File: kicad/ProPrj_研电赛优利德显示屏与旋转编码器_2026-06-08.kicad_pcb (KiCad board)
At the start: 2 copper layers, 75 x 45 mm, 16 parts, among them Q1 S8050, SW1 EC11N1525405, U1 ST7789_12P_LCD

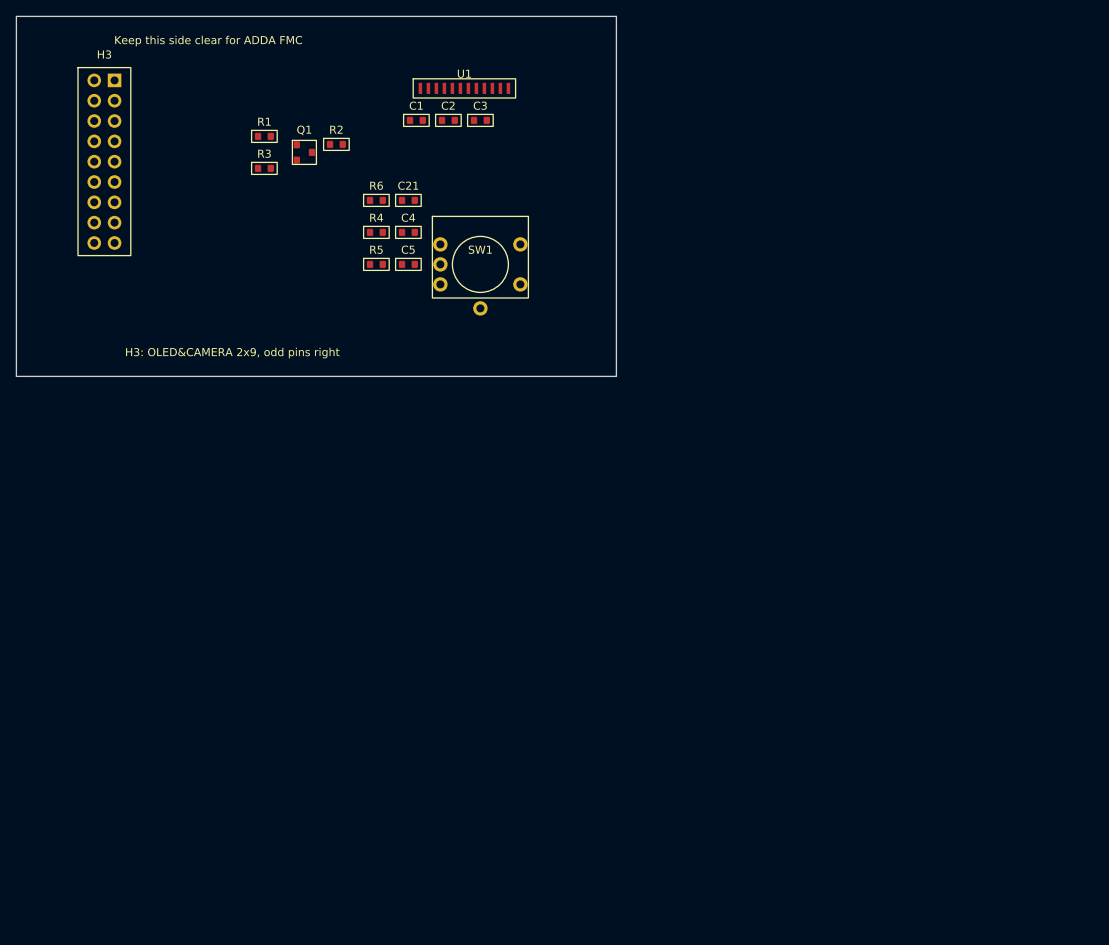
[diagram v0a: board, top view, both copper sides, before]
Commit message: perf: fix gated clock and DSP pipeline warnings
1. SPI gated clock (PDRC-153):
   - Replace posedge r_sclk with posedge clk_in + edge detection enable
   - Removes derived clock domain, uses main clk_in for all registers

2. DSP pipeline (DPIP-1/DPOP-2):
   - Add raw0_s1b..raw3_s1b pipeline registers between waveform mux and
     multiplier, enabling DSP48 AREG/BREG usage (DPIP-1: FIXED)
   - DPOP-2 (MREG) remains: DSP internal product register not used,
     timing still met at 250MHz

3. Results: 20 warnings -> 11 warnings
   - DSP: 8 -> 4 (DPIP-1 fixed, DPOP-2 remains minor)
   - Gated clock: 3 -> 3 (now false positive after fix)
   - ILA LUT/no-load: 6 -> 4 (Vivado IP internal, unfixable)

Co-Authored-By: Claude Opus 4.8 <noreply@anthropic.com>
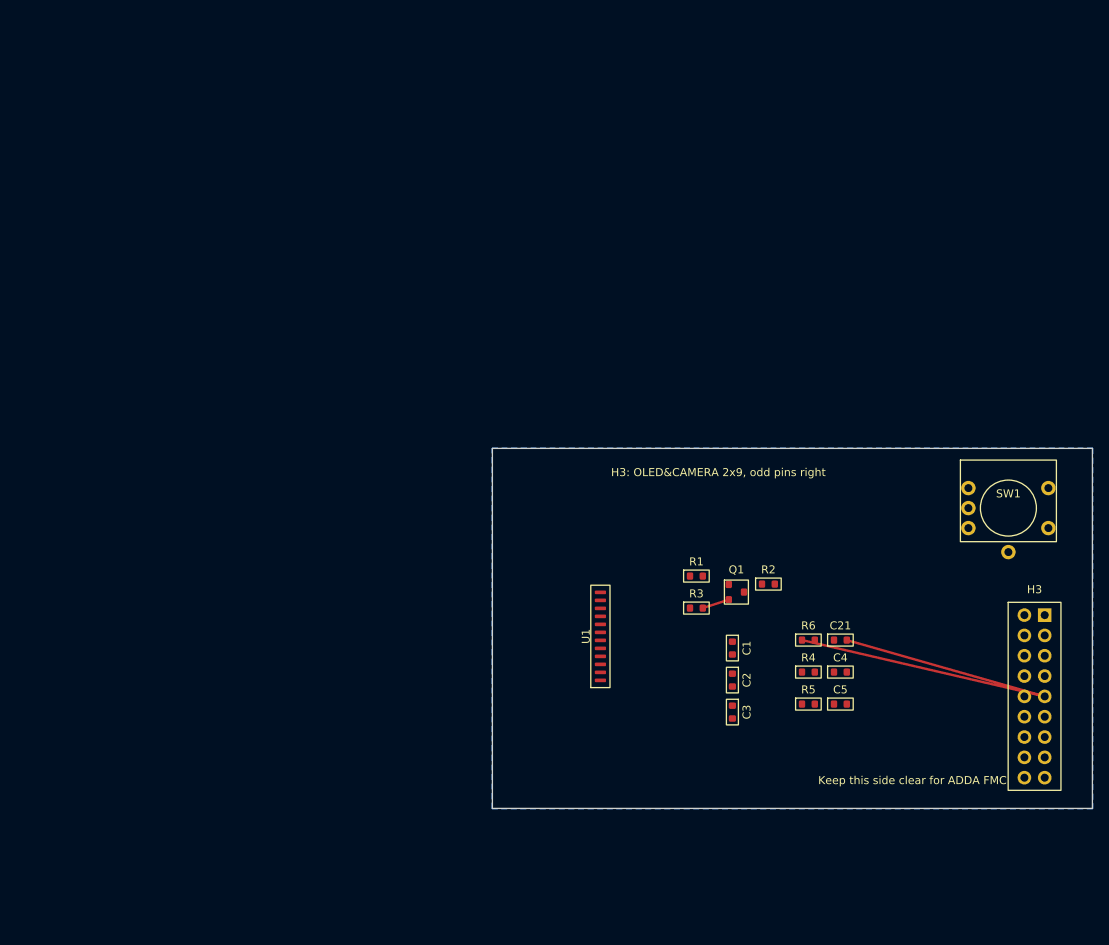
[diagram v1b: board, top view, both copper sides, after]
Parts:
- moved H3 134.1 mm to (127.3, 74.8)
- moved C3 80.4 mm to (89.5, 87.0), turned to -90 degrees
- moved C2 78.5 mm to (89.5, 83.0), turned to -90 degrees
- moved C21 77.0 mm to (103.0, 78.0)
- moved C4 77.0 mm to (103.0, 82.0)
- moved C5 77.0 mm to (103.0, 86.0)
- moved Q1 77.0 mm to (90.0, 72.0)
- moved R1 77.0 mm to (85.0, 70.0)
- moved R2 77.0 mm to (94.0, 71.0)
- moved R3 77.0 mm to (85.0, 74.0)
- moved R4 77.0 mm to (99.0, 82.0)
- moved R5 77.0 mm to (99.0, 86.0)
- moved R6 77.0 mm to (99.0, 78.0)
- moved C1 76.9 mm to (89.5, 79.0), turned to -90 degrees
- moved SW1 72.7 mm to (124.0, 61.5)
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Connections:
- net /TFT_BLK renamed TFT_BLK
- net /TFT_CS renamed TFT_CS
- net /TFT_DC renamed TFT_DC
- net /TFT_RES renamed TFT_RES
- net /TFT_SCL renamed TFT_SCL
- net /TFT_SDA renamed TFT_SDA
- H3 pad 10: /EC11-B -> EC11-B
- H3 pad 11: /EC11-M -> EC11-M
- H3 pad 12: /LEDK -> LEDK
- H3 pad 9: /EC11-A -> EC11-A
- SW1 pad A: /EC11-A -> EC11-A
- SW1 pad B: /EC11-B -> EC11-B
- SW1 pad D: /EC11-M -> EC11-M
- U1 pad 2: /LEDK -> LEDK
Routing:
- net /EC11-A: track 0.00 -> 56.9 mm
- net Net-(Q1-B): track 0.00 -> 3.42 mm
- added copper zone on B.Cu, net GND

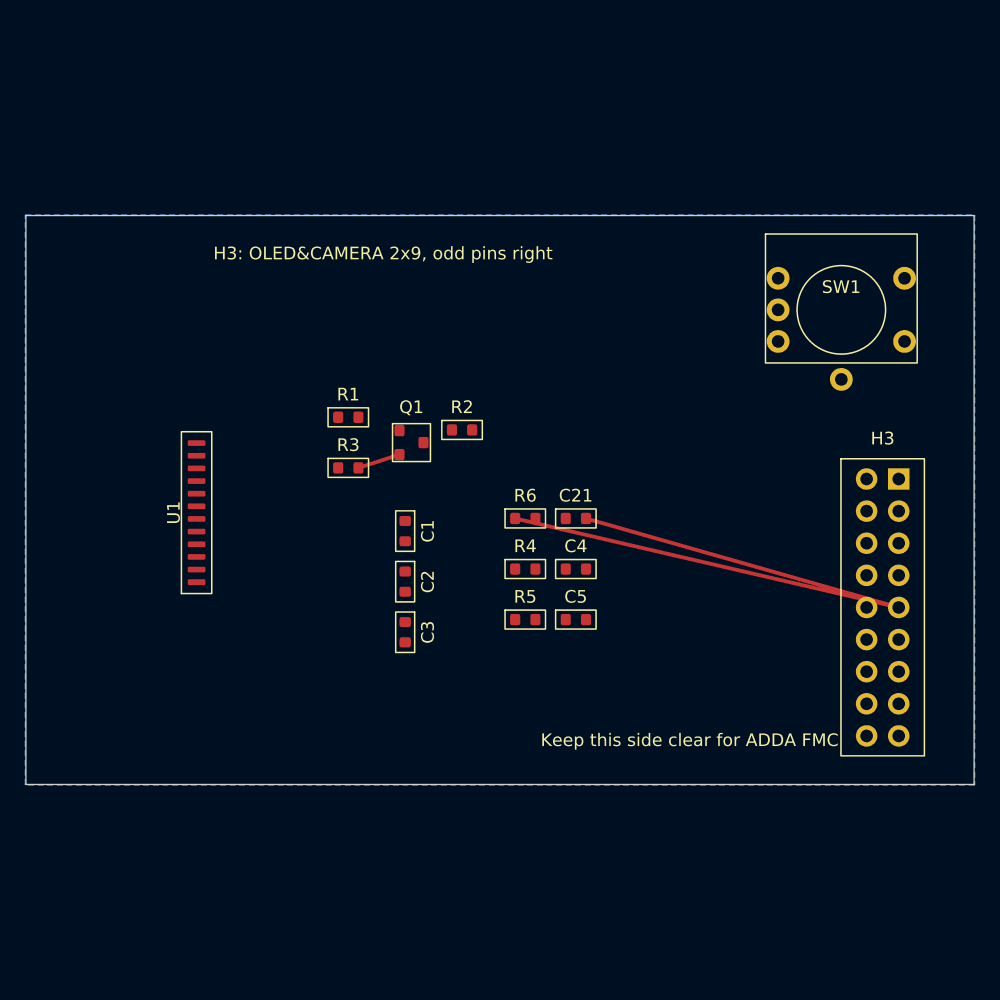
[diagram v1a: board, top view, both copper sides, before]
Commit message: perf: SPI robustness and obsidian cleanup
1. SPI gated clock: remove edge detector, use counter tick (spi_tick)
2. Suppress PDRC-153 (Vivado 2024.1 FSM false positive)
3. Remove 5 outdated obsidian docs (status/todo/roadmap from May 6)

Remaining 8 DRC warnings:
  - DPOP-2 x4: DSP MREG not used (timing met at 250MHz)
  - PDCN-1569 x3: ILA IP internal LUT (unfixable)
  - RTSTAT-10 x1: ILA debug hub (unfixable)

Bitstream generated: vivado/awg_k325t.runs/impl_1/awg_top.bit

Co-Authored-By: Claude Opus 4.8 <noreply@anthropic.com>
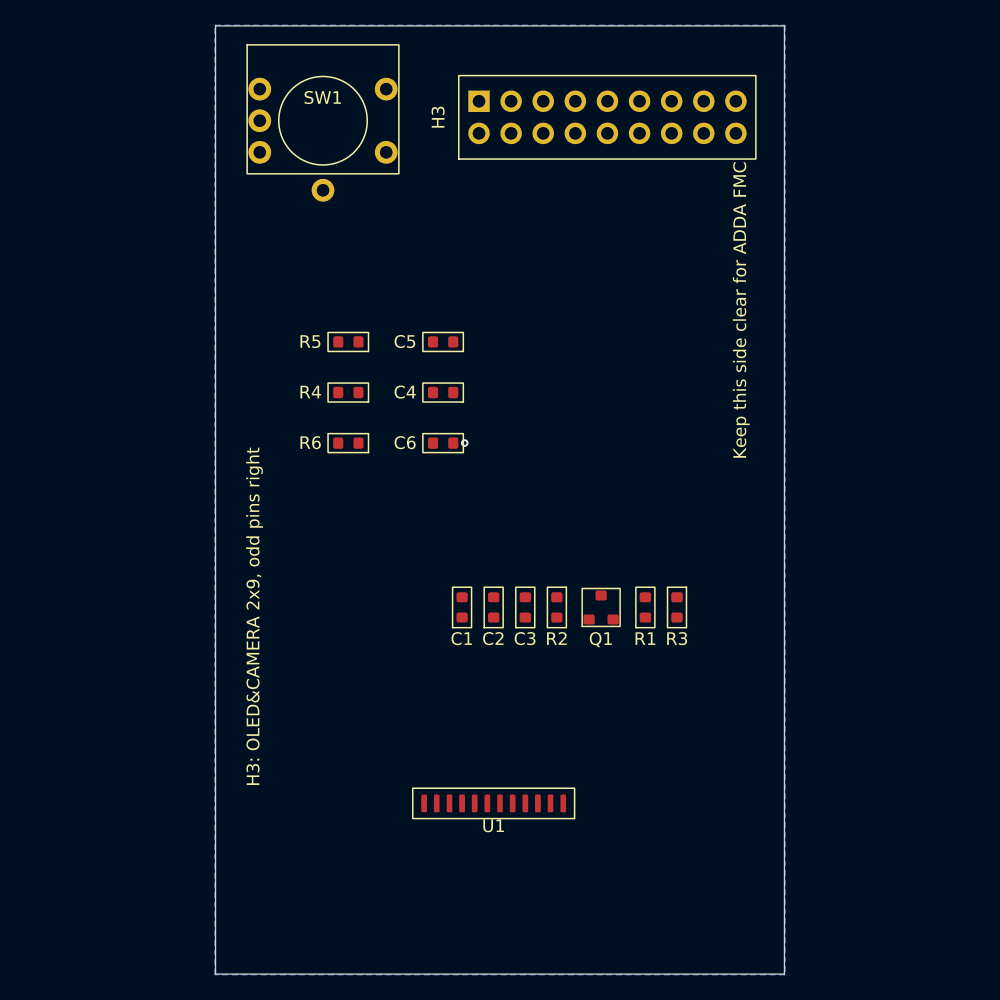
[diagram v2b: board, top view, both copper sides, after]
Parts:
- moved SW1 43.6 mm to (83.0, 46.5)
- moved H3 42.9 mm to (95.3, 46.2), turned to 90 degrees
- moved U1 32.9 mm to (96.5, 100.5), turned to 180 degrees
- moved R3 28.2 mm to (111.0, 85.0), turned to -90 degrees
- moved R1 27.9 mm to (108.5, 85.0), turned to 90 degrees
- moved R5 26.0 mm to (85.0, 64.0), turned to 180 degrees
- moved C5 24.3 mm to (92.5, 64.0), turned to 180 degrees
- moved Q1 19.9 mm to (105.0, 85.0), turned to 90 degrees
- moved R4 19.8 mm to (85.0, 68.0), turned to 180 degrees
- moved C4 17.5 mm to (92.5, 68.0), turned to 180 degrees
- moved R2 15.9 mm to (101.5, 85.0), turned to -90 degrees
- moved R6 15.2 mm to (85.0, 72.0), turned to 180 degrees
- moved C6 12.1 mm to (92.5, 72.0), turned to 180 degrees
- moved C3 9.70 mm to (99.0, 85.0), turned to 90 degrees
- moved C1 7.53 mm to (94.0, 85.0), turned to 90 degrees
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- renumbered C21 to C6
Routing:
- net /EC11-A: track 56.9 -> 0.00 mm
- net Net-(Q1-B): track 3.42 -> 0.00 mm
- net GND: vias 0 -> 1
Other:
- board size 75 x 45 mm -> 45 x 75 mm

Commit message: docs: add reference PDFs and verify all FMC pins
- Copy subcard user manual and baseboard schematic into docs/references/
- Track PDFs via Git LFS
- Cross-verify all 14 FMC signals against subcard manual: 14/14 MATCH
- Update fmc_adda_signal_map.md: all pins verified, status clean
- SPI robustness: replace edge-detected CE with counter tick

References now self-contained in the repo.

Co-Authored-By: Claude Opus 4.8 <noreply@anthropic.com>
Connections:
- C4 pad 2: /EC11-B -> EC11-B
- C5 pad 2: /EC11-M -> EC11-M
- C6 pad 2: /EC11-A -> EC11-A
- R4 pad 1: /EC11-B -> EC11-B
- R5 pad 1: /EC11-M -> EC11-M
- R6 pad 1: /EC11-A -> EC11-A
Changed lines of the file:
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@@
 			(layers "F.Cu" "F.Mask" "F.Paste")
 			(roundrect_rratio 0.2)
-			(net "/EC11-M")
+			(net "EC11-M")
 			(pinfunction "2")
 			(pintype "passive")
@@
 			(layers "F.Cu" "F.Mask" "F.Paste")
 			(roundrect_rratio 0.2)
-			(net "/EC11-A")
+			(net "EC11-A")
 			(pinfunction "2")
 			(pintype "passive")
@@
 			(layers "F.Cu" "F.Mask" "F.Paste")
 			(roundrect_rratio 0.2)
-			(net "/EC11-M")
+			(net "EC11-M")
 			(pinfunction "1")
 			(pintype "passive")
@@
 			(layers "F.Cu" "F.Mask" "F.Paste")
 			(roundrect_rratio 0.2)
-			(net "/EC11-B")
+			(net "EC11-B")
 			(pinfunction "1")
 			(pintype "passive")
@@
 			(layers "F.Cu" "F.Mask" "F.Paste")
 			(roundrect_rratio 0.2)
-			(net "/EC11-A")
+			(net "EC11-A")
 			(pinfunction "1")
 			(pintype "passive")
@@
 			(layers "F.Cu" "F.Mask" "F.Paste")
 			(roundrect_rratio 0.2)
-			(net "/EC11-B")
+			(net "EC11-B")
 			(pinfunction "2")
 			(pintype "passive")

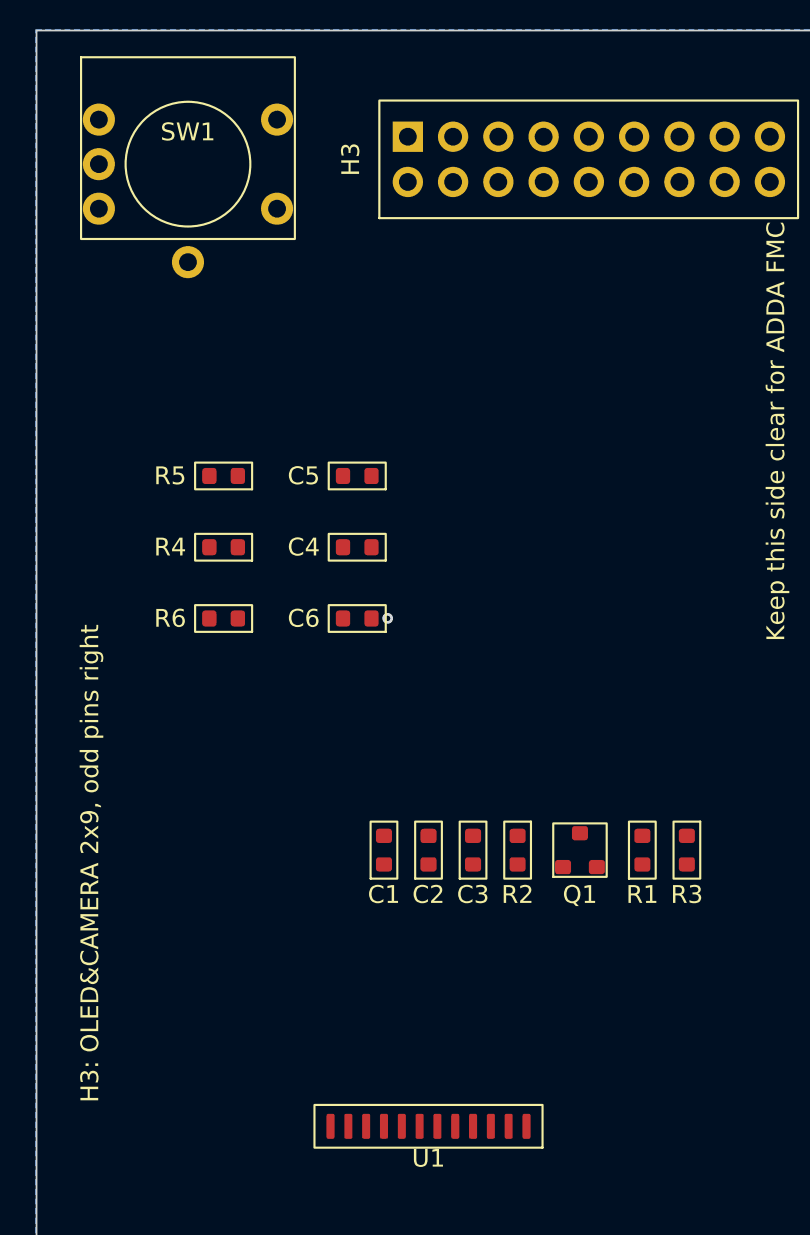
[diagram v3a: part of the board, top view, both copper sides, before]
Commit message: docs: consolidate obsidian into docs/
Move 16 technical documents from obsidian/ to docs/ subdirectories:
  overview/       - 项目概述、硬件平台、工具链
  architecture/   - 顶层架构图、时钟树
  modules/        - AD9144/JESD/LMK/DDS 设计笔记
  timing/         - 约束速查、CDC 风险
  troubleshooting/ - License/错误/验证流程
  reference/      - 参数手册、文件索引

- Remove obsidian frontmatter from all files
- Fix outdated path references
- Update README to reflect new doc structure
- Delete obsidian/ directory

Co-Authored-By: Claude Opus 4.8 <noreply@anthropic.com>
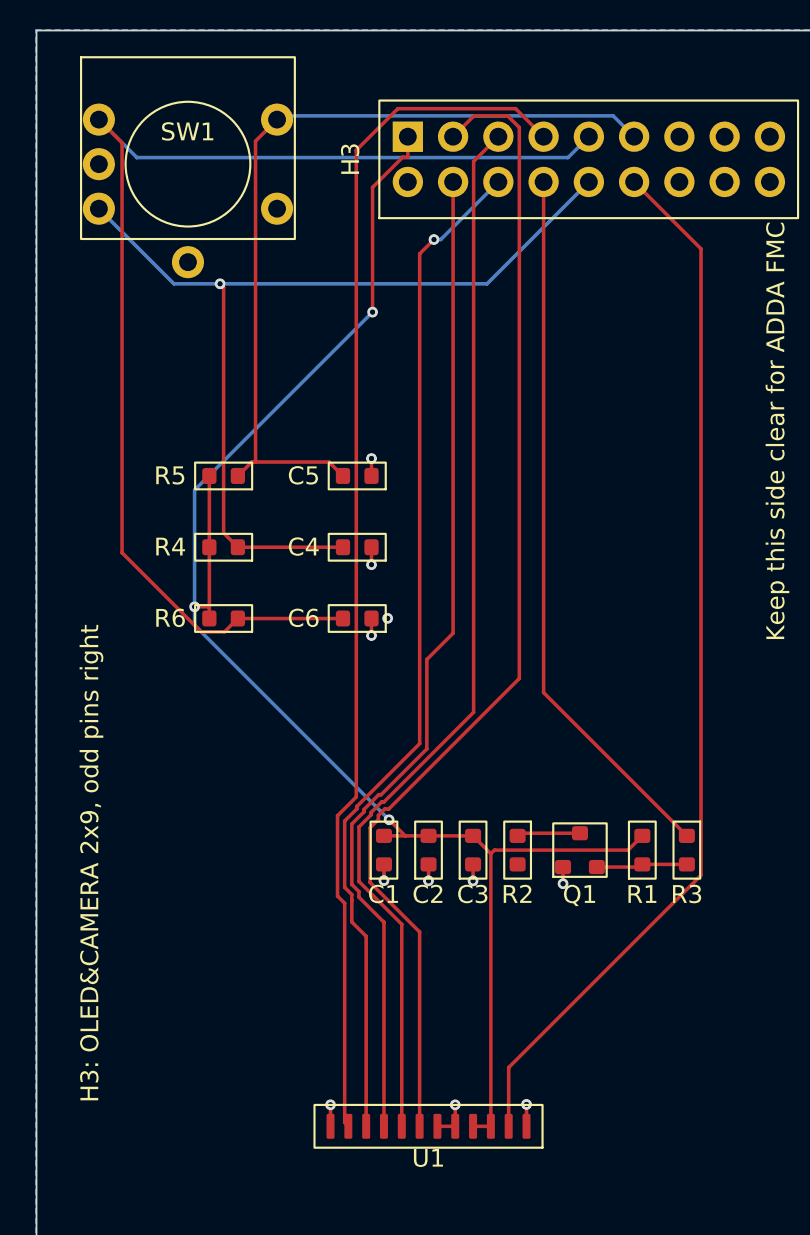
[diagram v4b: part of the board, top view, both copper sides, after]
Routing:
- net VCC: track 0.00 -> 89.7 mm, vias 0 -> 3
- net EC11-A: track 0.00 -> 68.3 mm
- net TFT_RES: track 0.00 -> 67.6 mm
- net TFT_DC: track 0.00 -> 65.3 mm
- net TFT_CS: track 0.00 -> 59.9 mm
- net LEDK: track 0.00 -> 59.0 mm
- net TFT_SDA: track 0.00 -> 57.3 mm, vias 0 -> 1
- net TFT_SCL: track 0.00 -> 56.2 mm
- net EC11-B: track 0.00 -> 52.7 mm, vias 0 -> 1
- net EC11-M: track 0.00 -> 46.9 mm
- net TFT_BLK: track 0.00 -> 40.0 mm
- net GND: track 0.00 -> 11.3 mm, vias 1 -> 11
- net Net-(Q1-B): track 0.00 -> 5.11 mm
- net Net-(Q1-C): track 0.00 -> 3.56 mm
